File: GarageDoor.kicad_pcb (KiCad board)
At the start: 2 copper layers, 90 x 70 mm, 32 parts, among them J1 1935161.0, J2 EB21A-04-C, J3 EB21A-04-C, K1 SRD-12VDC-SL-C, K2 SRD-12VDC-SL-C, Q1 BS170-D26Z, Q2 BS170-D26Z, Q3 IRFR9024NTRLPBF, U1 LM2596, U2 WeMos_D1_mini

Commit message: Connect unused pins to ground.
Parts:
- removed G***: LOGO, Graphics:Nlogo_10mm_x_10mm
- removed REF**: OSHW-Symbol_6.7x6mm_SilkScreen, Symbol:OSHW-Symbol_6.7x6mm_SilkScreen
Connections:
- U2 pad 1: unconnected-(U2-Rst-Pad1) -> Earth
- U2 pad 11: unconnected-(U2-2(LED)-Pad11) -> Earth
- U2 pad 12: unconnected-(U2-0-Pad12) -> Earth
- U2 pad 15: unconnected-(U2-Rx-Pad15) -> Earth
- U2 pad 16: unconnected-(U2-Tx-Pad16) -> Earth
- U2 pad 2: unconnected-(U2-A0-Pad2) -> Earth
- U2 pad 5: unconnected-(U2-12/MISO-Pad5) -> Earth
- U2 pad 6: unconnected-(U2-13/MOSI-Pad6) -> Earth
- U2 pad 7: unconnected-(U2-15-Pad7) -> Earth
- U2 pad 8: unconnected-(U2-3.3V-Pad8) -> Earth

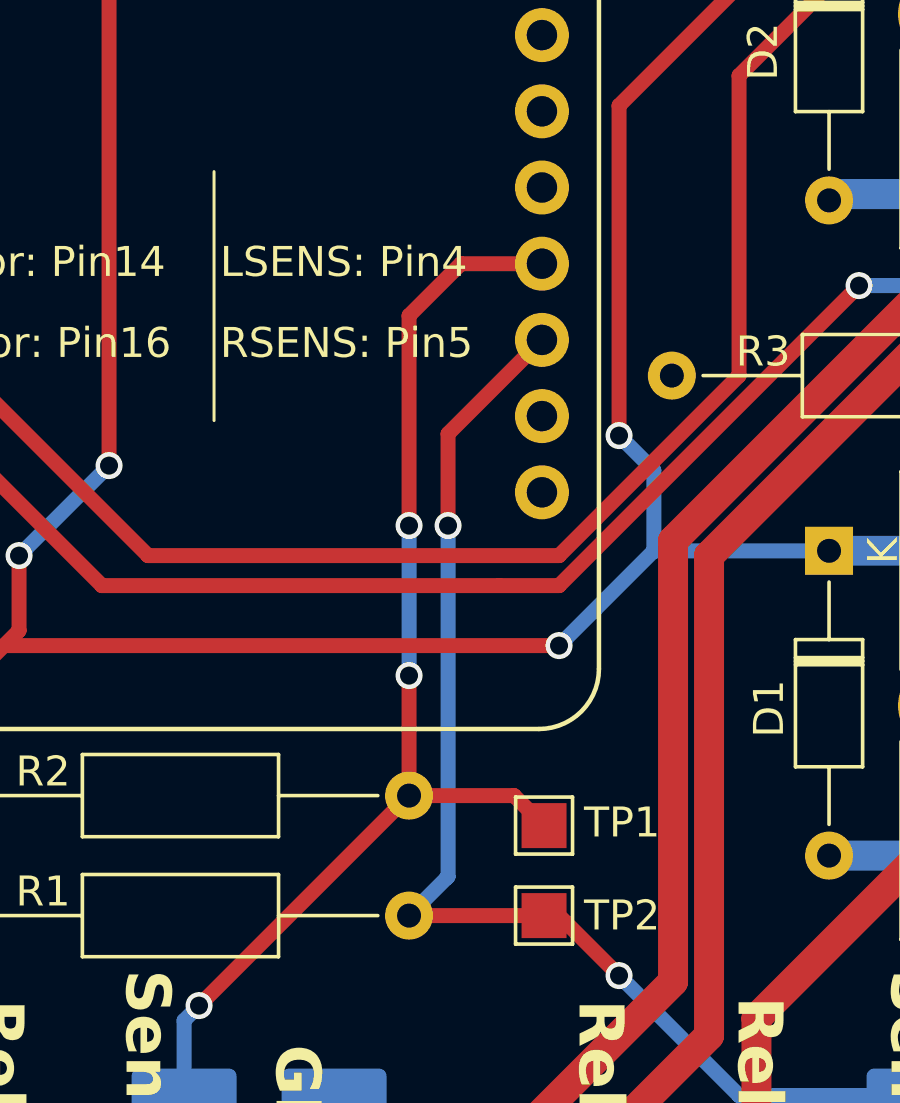
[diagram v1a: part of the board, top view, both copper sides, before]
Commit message: Move right sensor to pin 12 instead of 16, because that breaks everything for some reason and you're apparently just supposed to know that.
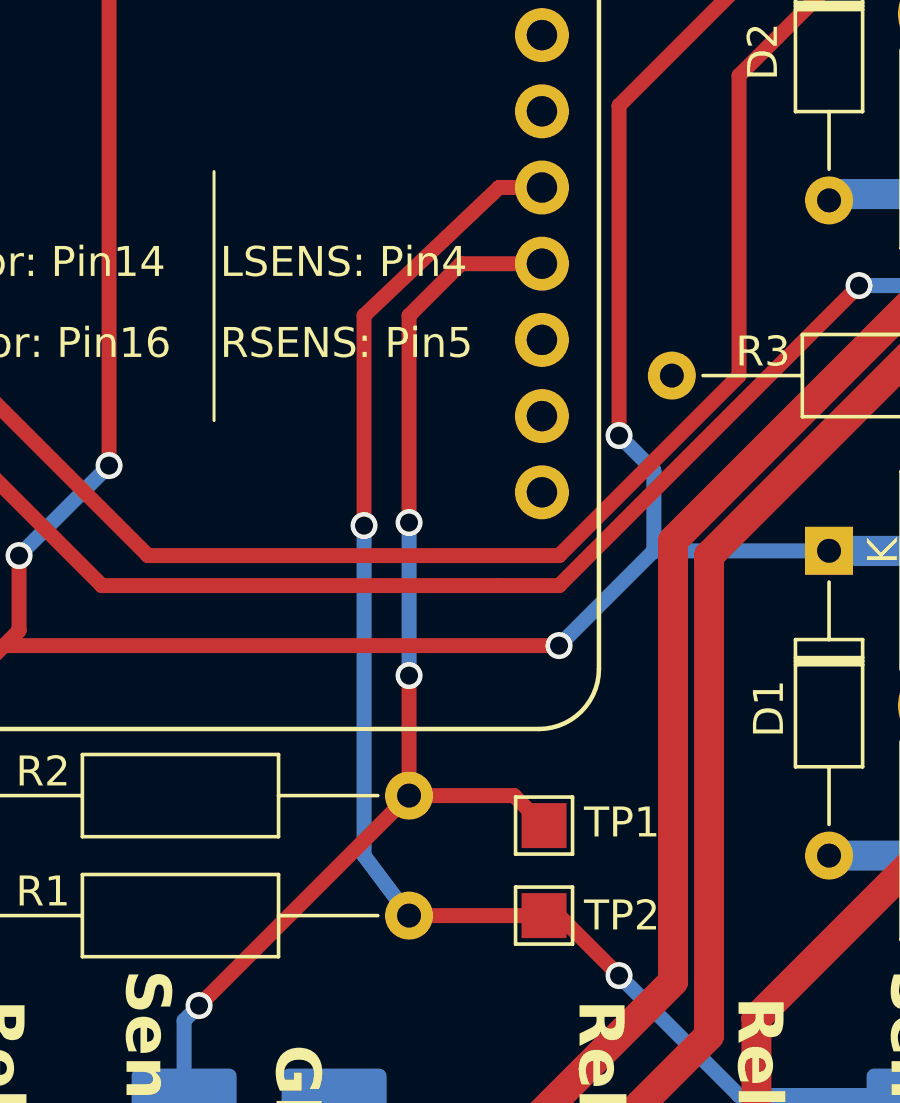
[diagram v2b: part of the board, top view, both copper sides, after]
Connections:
- U2 pad 1: Earth -> unconnected-(U2-Rst-Pad1)
- U2 pad 11: Earth -> unconnected-(U2-2(LED)-Pad11)
- U2 pad 12: Earth -> unconnected-(U2-0-Pad12)
- U2 pad 15: Earth -> unconnected-(U2-Rx-Pad15)
- U2 pad 16: Earth -> unconnected-(U2-Tx-Pad16)
- U2 pad 2: Earth -> unconnected-(U2-A0-Pad2)
- U2 pad 3: RIGHT_SENSOR -> unconnected-(U2-16-Pad3)
- U2 pad 5: Earth -> RIGHT_SENSOR
- U2 pad 6: Earth -> unconnected-(U2-13/MOSI-Pad6)
- U2 pad 7: Earth -> unconnected-(U2-15-Pad7)
- U2 pad 8: Earth -> unconnected-(U2-3.3V-Pad8)
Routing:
- net RIGHT_SENSOR: track 47.7 -> 54.8 mm
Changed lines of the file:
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@@
   (net 18 "unconnected-(K2-Pad4)")
   (net 19 "Net-(D3-A1)")
+  (net 20 "unconnected-(U2-Rst-Pad1)")
+  (net 21 "unconnected-(U2-A0-Pad2)")
+  (net 22 "unconnected-(U2-16-Pad3)")
+  (net 23 "unconnected-(U2-13{slash}MOSI-Pad6)")
+  (net 24 "unconnected-(U2-15-Pad7)")
+  (net 25 "unconnected-(U2-3.3V-Pad8)")
+  (net 26 "unconnected-(U2-2(LED)-Pad11)")
+  (net 27 "unconnected-(U2-0-Pad12)")
+  (net 28 "unconnected-(U2-Rx-Pad15)")
+  (net 29 "unconnected-(U2-Tx-Pad16)")
   (footprint "TestPoint:TestPoint_Pad_1.5x1.5mm" (layer "F.Cu")
     (at 80.5 75)
@@
       (stroke (width 0.05) (type solid)) (layer "F.CrtYd"))
     (pad "1" thru_hole circle (at 8.89 -11.43 270) (size 1.8 1.8) (drill 1.016) (layers "*.Cu" "*.Mask")
-      (net 4 "Earth") (pinfunction "Rst") (pintype "bidirectional"))
+      (net 20 "unconnected-(U2-Rst-Pad1)") (pinfunction "Rst") (pintype "bidirectional+no_connect"))
     (pad "2" thru_hole circle (at 6.35 -11.43 270) (size 1.8 1.8) (drill 1.016) (layers "*.Cu" "*.Mask")
-      (net 4 "Earth") (pinfunction "A0") (pintype "bidirectional"))
+      (net 21 "unconnected-(U2-A0-Pad2)") (pinfunction "A0") (pintype "bidirectional+no_connect"))
     (pad "3" thru_hole circle (at 3.81 -11.43 270) (size 1.8 1.8) (drill 1.016) (layers "*.Cu" "*.Mask")
-      (net 6 "RIGHT_SENSOR") (pinfunction "16") (pintype "bidirectional"))
+      (net 22 "unconnected-(U2-16-Pad3)") (pinfunction "16") (pintype "bidirectional+no_connect"))
     (pad "4" thru_hole circle (at 1.27 -11.43 270) (size 1.8 1.8) (drill 1.016) (layers "*.Cu" "*.Mask")
       (net 5 "LEFT_SENSOR") (pinfunction "14/SCK") (pintype "bidirectional"))
     (pad "5" thru_hole circle (at -1.27 -11.43 270) (size 1.8 1.8) (drill 1.016) (layers "*.Cu" "*.Mask")
-      (net 4 "Earth") (pinfunction "12/MISO") (pintype "bidirectional"))
+      (net 6 "RIGHT_SENSOR") (pinfunction "12/MISO") (pintype "bidirectional"))
     (pad "6" thru_hole circle (at -3.81 -11.43) (size 1.8 1.8) (drill 1.016) (layers "*.Cu" "*.Mask")
-      (net 4 "Earth") (pinfunction "13/MOSI") (pintype "bidirectional"))
+      (net 23 "unconnected-(U2-13{slash}MOSI-Pad6)") (pinfunction "13/MOSI") (pintype "bidirectional+no_connect"))
     (pad "7" thru_hole circle (at -6.35 -11.43 270) (size 1.8 1.8) (drill 1.016) (layers "*.Cu" "*.Mask")
-      (net 4 "Earth") (pinfunction "15") (pintype "bidirectional"))
+      (net 24 "unconnected-(U2-15-Pad7)") (pinfunction "15") (pintype "bidirectional+no_connect"))
     (pad "8" thru_hole circle (at -8.89 -11.43 270) (size 1.8 1.8) (drill 1.016) (layers "*.Cu" "*.Mask")
-      (net 4 "Earth") (pinfunction "3.3V") (pintype "power_out"))
+      (net 25 "unconnected-(U2-3.3V-Pad8)") (pinfunction "3.3V") (pintype "power_out+no_connect"))
     (pad "9" thru_hole circle (at -8.89 11.43 270) (size 1.8 1.8) (drill 1.016) (layers "*.Cu" "*.Mask")
       (net 12 "+5V") (pinfunction "5V") (pintype "power_in"))
@@
       (net 4 "Earth") (pinfunction "GND") (pintype "power_in"))
     (pad "11" thru_hole circle (at -3.81 11.43 270) (size 1.8 1.8) (drill 1.016) (layers "*.Cu" "*.Mask")
-      (net 4 "Earth") (pinfunction "2(LED)") (pintype "bidirectional"))
+      (net 26 "unconnected-(U2-2(LED)-Pad11)") (pinfunction "2(LED)") (pintype "bidirectional+no_connect"))
     (pad "12" thru_hole circle (at -1.27 11.43 270) (size 1.8 1.8) (drill 1.016) (layers "*.Cu" "*.Mask")
-      (net 4 "Earth") (pinfunction "0") (pintype "bidirectional"))
+      (net 27 "unconnected-(U2-0-Pad12)") (pinfunction "0") (pintype "bidirectional+no_connect"))
     (pad "13" thru_hole circle (at 1.27 11.43 270) (size 1.8 1.8) (drill 1.016) (layers "*.Cu" "*.Mask")
       (net 14 "Net-(Q2-G)") (pinfunction "4/SDA") (pintype "bidirectional"))
@@
       (net 13 "Net-(Q1-G)") (pinfunction "5/SCL") (pintype "bidirectional"))
     (pad "15" thru_hole circle (at 6.35 11.43 270) (size 1.8 1.8) (drill 1.016) (layers "*.Cu" "*.Mask")
-      (net 4 "Earth") (pinfunction "Rx") (pintype "bidirectional"))
+      (net 28 "unconnected-(U2-Rx-Pad15)") (pinfunction "Rx") (pintype "bidirectional+no_connect"))
     (pad "16" thru_hole circle (at 8.89 11.43 270) (size 1.8 1.8) (drill 1.016) (layers "*.Cu" "*.Mask")
-      (net 4 "Earth") (pinfunction "Tx") (pintype "bidirectional"))
+      (net 29 "unconnected-(U2-Tx-Pad16)") (pinfunction "Tx") (pintype "bidirectional+no_connect"))
     (model "${KIPRJMOD}/3dshapes/wemos_d1_mini.3dshapes/d1_mini_shield.wrl"
       (offset (xyz -17.89999973 -12.79999981 8.399999874))
@@
   (segment (start 76 74) (end 76 70) (width 0.5) (layer "F.Cu") (net 5))
   (segment (start 69 81) (end 76 74) (width 0.5) (layer "F.Cu") (net 5))
+  (segment (start 76 64.9) (end 76 58) (width 0.5) (layer "F.Cu") (net 5))
   (segment (start 77.73 56.27) (end 80.43 56.27) (width 0.5) (layer "F.Cu") (net 5))
+  (segment (start 79.5 74) (end 80.5 75) (width 0.5) (layer "F.Cu") (net 5))
   (segment (start 76 58) (end 77.73 56.27) (width 0.5) (layer "F.Cu") (net 5))
-  (segment (start 76 65) (end 76 58) (width 0.5) (layer "F.Cu") (net 5))
-  (segment (start 79.5 74) (end 80.5 75) (width 0.5) (layer "F.Cu") (net 5))
   (via (at 69 81) (size 0.9) (drill 0.6) (layers "F.Cu" "B.Cu") (net 5))
-  (via (at 76 65) (size 0.9) (drill 0.6) (layers "F.Cu" "B.Cu") (net 5))
+  (via (at 76 64.9) (size 0.9) (drill 0.6) (layers "F.Cu" "B.Cu") (net 5))
   (via (at 76 70) (size 0.9) (drill 0.6) (layers "F.Cu" "B.Cu") (net 5))
   (segment (start 68.5 89.88) (end 67.38 91) (width 1) (layer "B.Cu") (net 5))
   (segment (start 68.5 81.5) (end 69 81) (width 0.5) (layer "B.Cu") (net 5))
   (segment (start 68.5 84) (end 68.5 81.5) (width 0.5) (layer "B.Cu") (net 5))
-  (segment (start 76 70) (end 76 65) (width 0.5) (layer "B.Cu") (net 5))
+  (segment (start 76 70) (end 76 64.9) (width 0.5) (layer "B.Cu") (net 5))
   (segment (start 68.5 84) (end 68.5 89.88) (width 1) (layer "B.Cu") (net 5))
-  (segment (start 77.3 65) (end 77.3 61.94) (width 0.5) (layer "F.Cu") (net 6))
+  (segment (start 74.5 58) (end 79 53.73) (width 0.5) (layer "F.Cu") (net 6))
   (segment (start 81 78) (end 76 78) (width 0.5) (layer "F.Cu") (net 6))
-  (segment (start 77.3 61.94) (end 80.43 58.81) (width 0.5) (layer "F.Cu") (net 6))
+  (segment (start 74.5 65) (end 74.5 58) (width 0.5) (layer "F.Cu") (net 6))
+  (segment (start 79 53.73) (end 80.43 53.73) (width 0.5) (layer "F.Cu") (net 6))
   (segment (start 83 80) (end 81 78) (width 0.5) (layer "F.Cu") (net 6))
+  (via (at 74.5 65) (size 0.9) (drill 0.6) (layers "F.Cu" "B.Cu") (net 6))
   (via (at 83 80) (size 0.9) (drill 0.6) (layers "F.Cu" "B.Cu") (net 6))
-  (via (at 77.3 65) (size 0.9) (drill 0.6) (layers "F.Cu" "B.Cu") (net 6))
-  (segment (start 77.3 76.7) (end 77.3 65) (width 0.5) (layer "B.Cu") (net 6))
   (segment (start 87 84) (end 93 84) (width 0.5) (layer "B.Cu") (net 6))
+  (segment (start 74.5 65) (end 74.5 76) (width 0.5) (layer "B.Cu") (net 6))
   (segment (start 93 90.66) (end 92.66 91) (width 1) (layer "B.Cu") (net 6))
-  (segment (start 76 78) (end 77.25 76.75) (width 0.5) (layer "B.Cu") (net 6))
-  (segment (start 77.25 76.75) (end 77.3 76.7) (width 0.5) (layer "B.Cu") (net 6))
   (segment (start 83 80) (end 87 84) (width 0.5) (layer "B.Cu") (net 6))
+  (segment (start 74.5 76) (end 76 78) (width 0.5) (layer "B.Cu") (net 6))
   (segment (start 93 84) (end 93 90.66) (width 1) (layer "B.Cu") (net 6))
   (segment (start 86 82) (end 86 66) (width 1) (layer "F.Cu") (net 7))

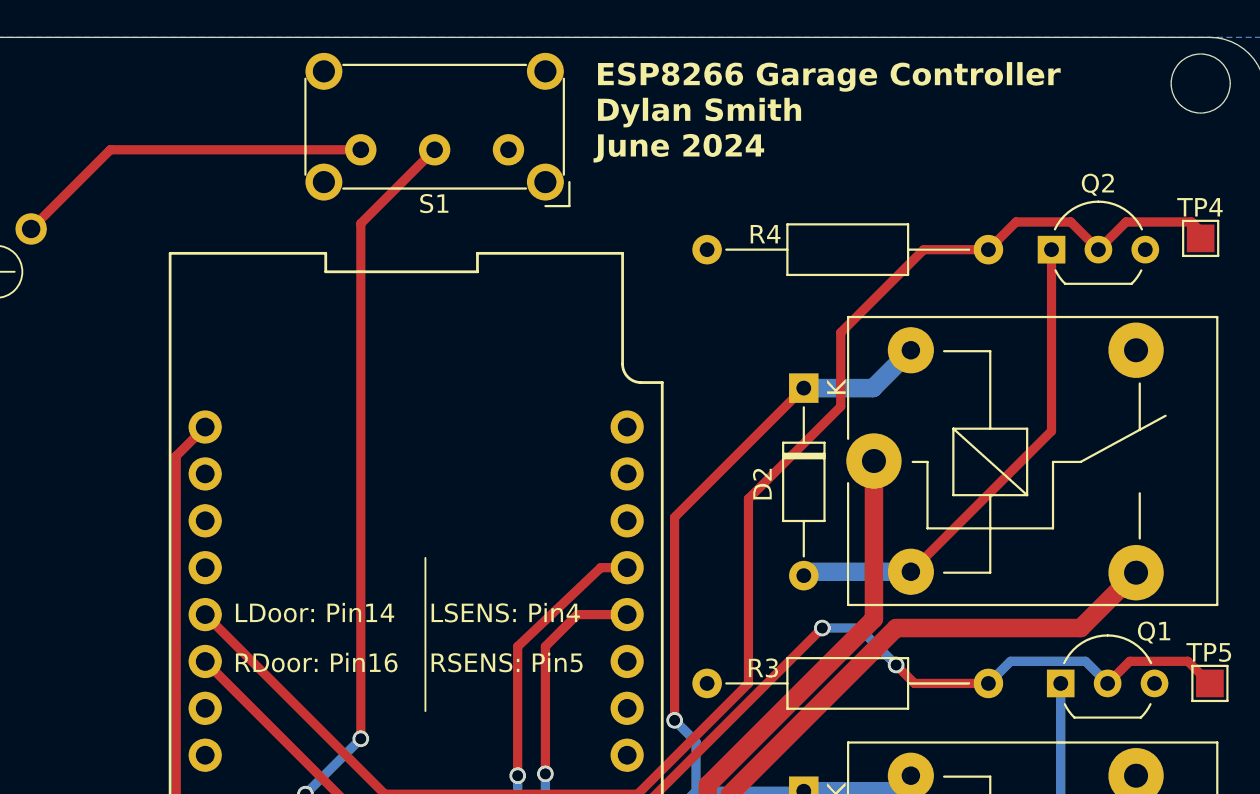
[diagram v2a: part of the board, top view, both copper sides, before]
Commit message: Minor silkscreen change
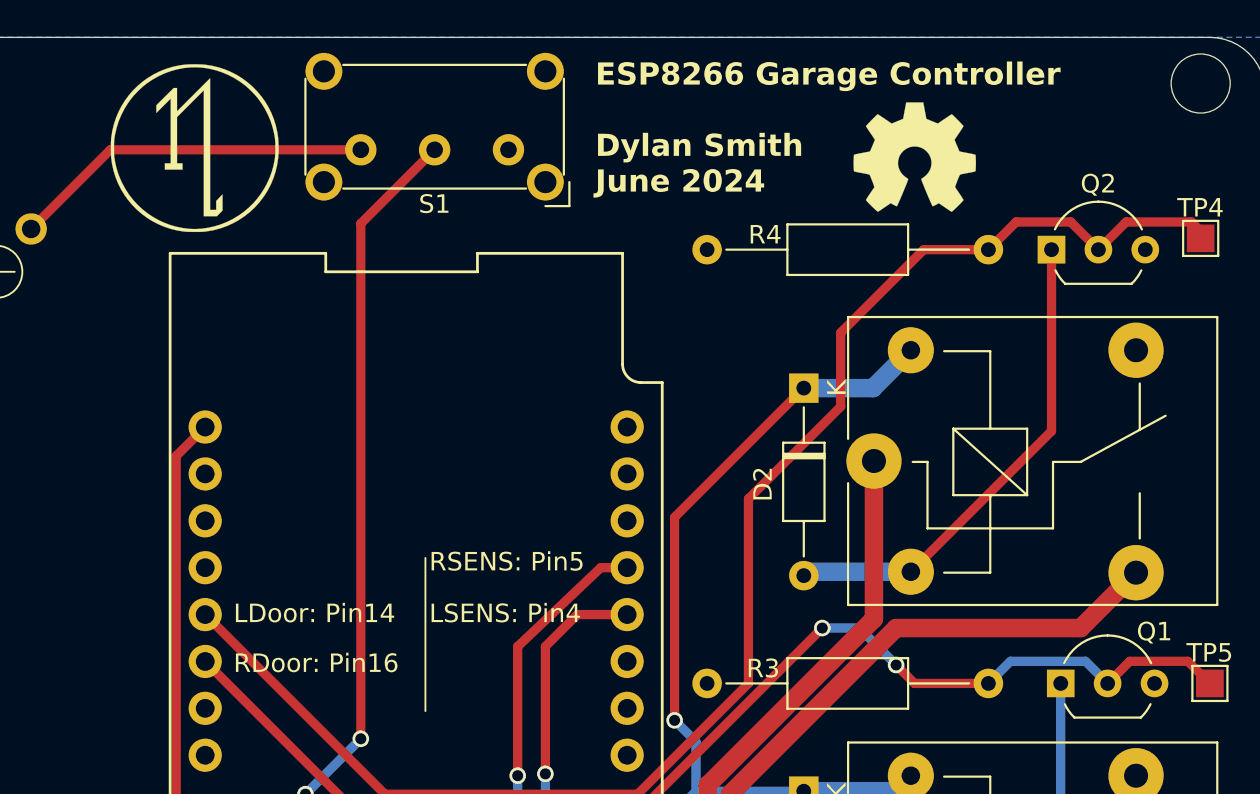
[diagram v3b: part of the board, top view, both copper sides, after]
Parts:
- added G***: LOGO, Graphics:Nlogo_10mm_x_10mm, F.Cu at (57.0, 31.0)
- added REF**: OSHW-Symbol_6.7x6mm_SilkScreen, Symbol:OSHW-Symbol_6.7x6mm_SilkScreen, F.Cu at (96.0, 31.5)

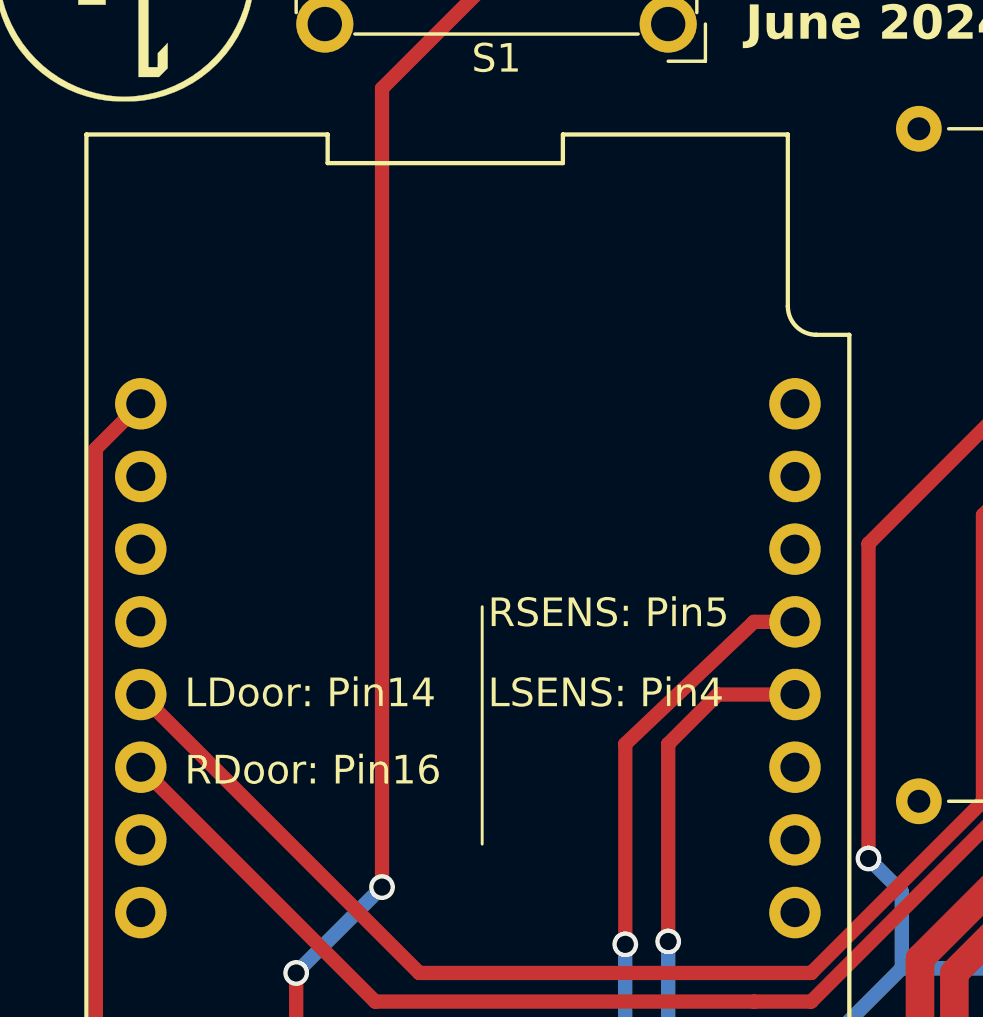
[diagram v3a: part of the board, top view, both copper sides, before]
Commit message: Correct silkscreen. Update to Kicad 8.
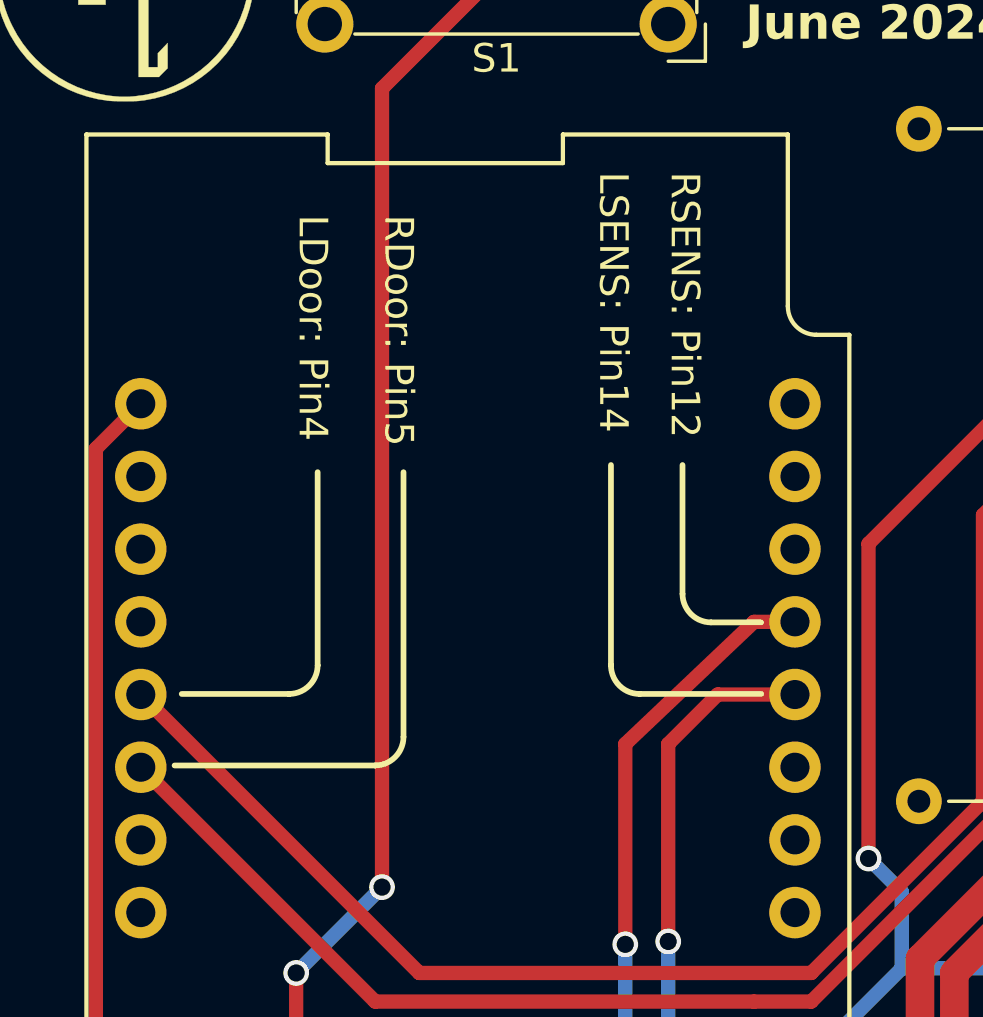
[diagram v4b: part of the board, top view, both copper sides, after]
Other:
- board text added: "LDoor: Pin4"
- board text added: "LSENS: Pin14"
- board text added: "RDoor: Pin5"
- board text added: "RSENS: Pin12"
- board text removed: "LDoor: Pin14"
- board text removed: "LSENS: Pin4"
- board text removed: "RDoor: Pin16"
- board text removed: "RSENS: Pin5"
